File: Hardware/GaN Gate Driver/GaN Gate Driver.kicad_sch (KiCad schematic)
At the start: 12 parts, among them J1 3296W-1-102LF, U1 LT1804

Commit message: Updating Schematic
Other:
- company: (none) -> OpenEPR
- title: (none) -> GaN Gate Driver
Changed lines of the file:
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@@
 	(generator_version "8.0")
 	(paper "A4")
+	(title_block
+		(title "GaN Gate Driver")
+		(date "2024-06-16")
+		(rev "v1.0")
+		(company "OpenEPR")
+		(comment 1 "Timothy Keller")
+	)
 	(junction
 		(at 50.8 60.96)

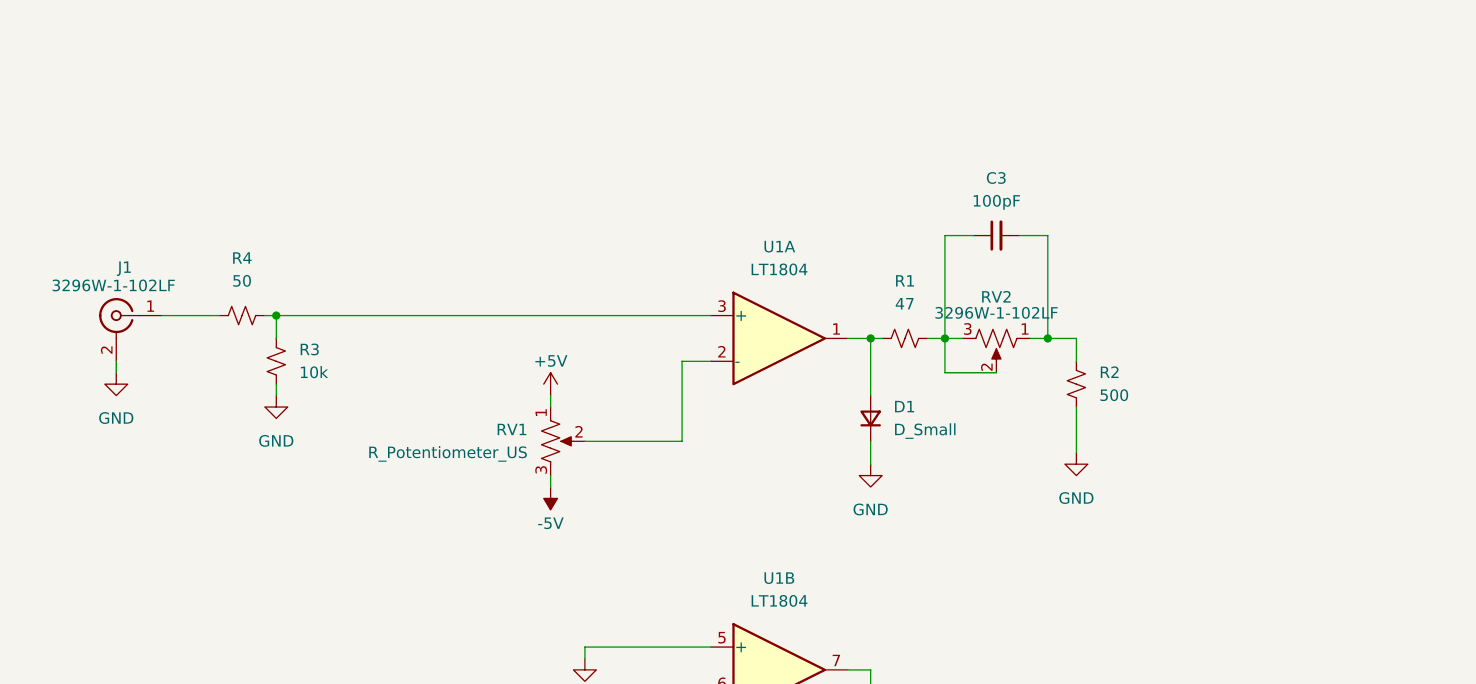
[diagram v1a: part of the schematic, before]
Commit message: Updates to gate driver
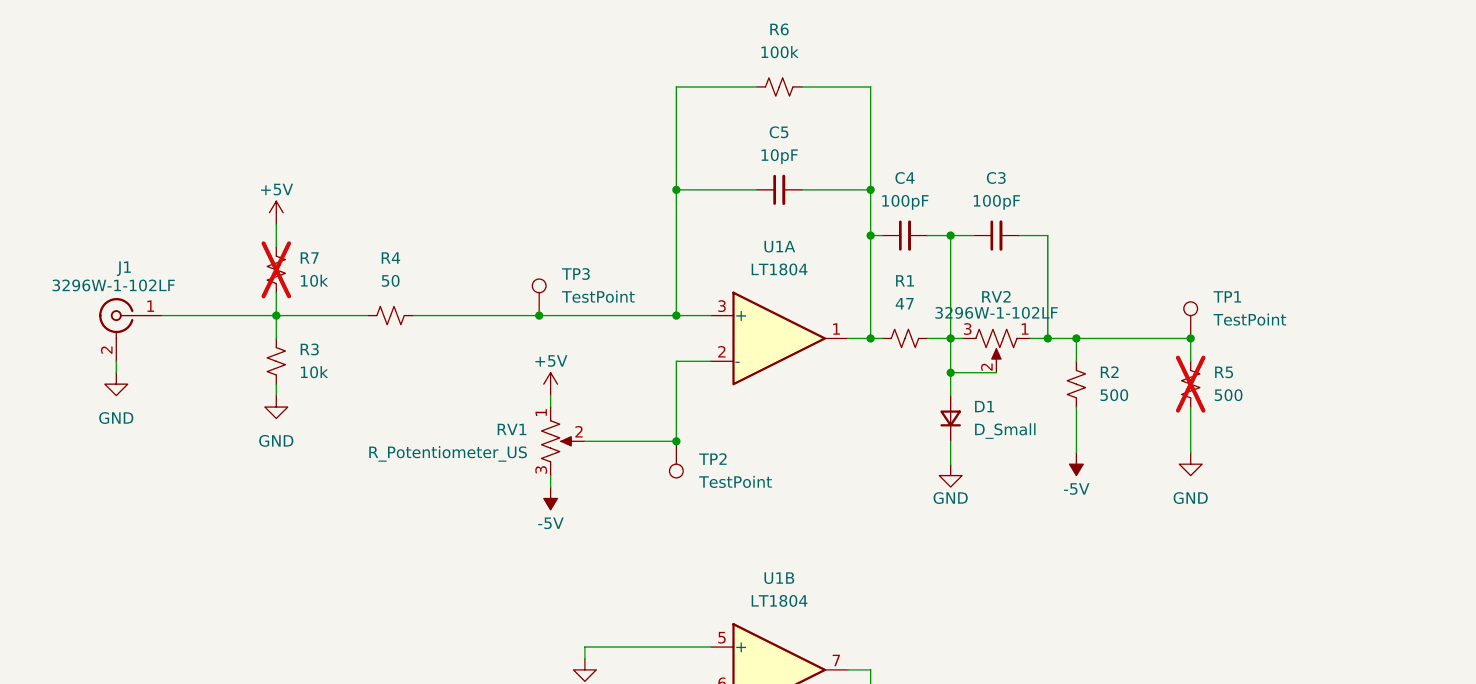
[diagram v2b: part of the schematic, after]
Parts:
- added C4: 100pF, Capacitor_SMD:C_0805_2012Metric, symbol Device:C_Small
- added C5: 10pF, Capacitor_SMD:C_0805_2012Metric, symbol Device:C_Small
- added R5: 500, Resistor_SMD:R_0805_2012Metric, symbol Device:R_Small_US
- added R6: 100k, Resistor_SMD:R_0805_2012Metric, symbol Device:R_Small_US
- added R7: 10k, Resistor_SMD:R_0805_2012Metric, symbol Device:R_Small_US
- added TP1, TP2, TP3: TestPoint, symbol Connector:TestPoint
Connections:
- net +5V: now also R7.2
- net -5V: now also R2.1
- net GND: now also R5.1; no longer R2.1
- net at R1.1, U1.1: now also C4.1, C5.2, R6.2; no longer D1.2 (A)
- net at C3.2, R2.2, RV2.1: now also R5.2, TP1.1
- net at C3.1, R1.2, RV2.2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: now also D1.2 (A), C4.2
- net at J1.1 (In), R4.1: now also R3.2, R7.1
- net at R4.2, U1.3 (+): now also C5.1, R6.1, TP3.1; no longer R3.2
- net at RV1.2, U1.2 (-): now also TP2.1
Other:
- moved on the sheet: D1, R4

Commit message: Updates to gate driver
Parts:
- added H1, H2, H3, H4: 4-40, _tim-Mounting-Holes:4-40_Hole_Pad, symbol Mechanical:MountingHole_Pad
- added J2: Conn_01x03_Socket, symbol Connector:Conn_01x03_Socket
- TP1, TP2, TP3: footprint (none) -> TestPoint:TestPoint_Pad_D1.0mm
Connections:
- net +5V: now also J2.1 (Pin_1)
- net -5V: now also J2.3 (Pin_3)
- net GND: now also H1.1, H2.1, H3.1, H4.1, J2.2 (Pin_2)

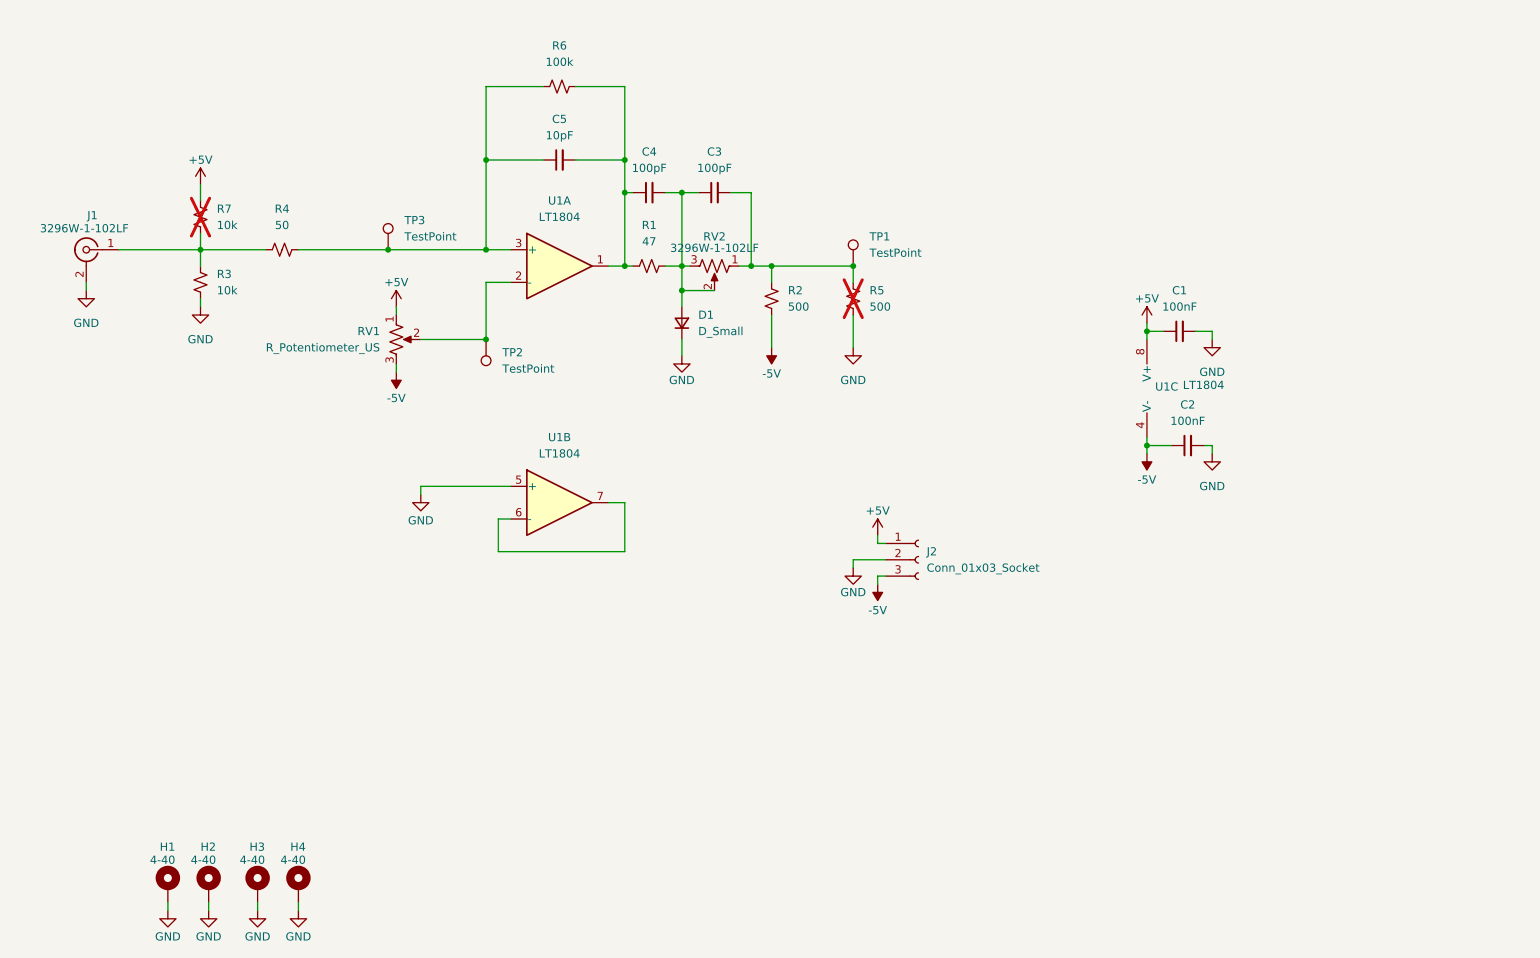
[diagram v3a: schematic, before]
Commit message: Updating gate driver board
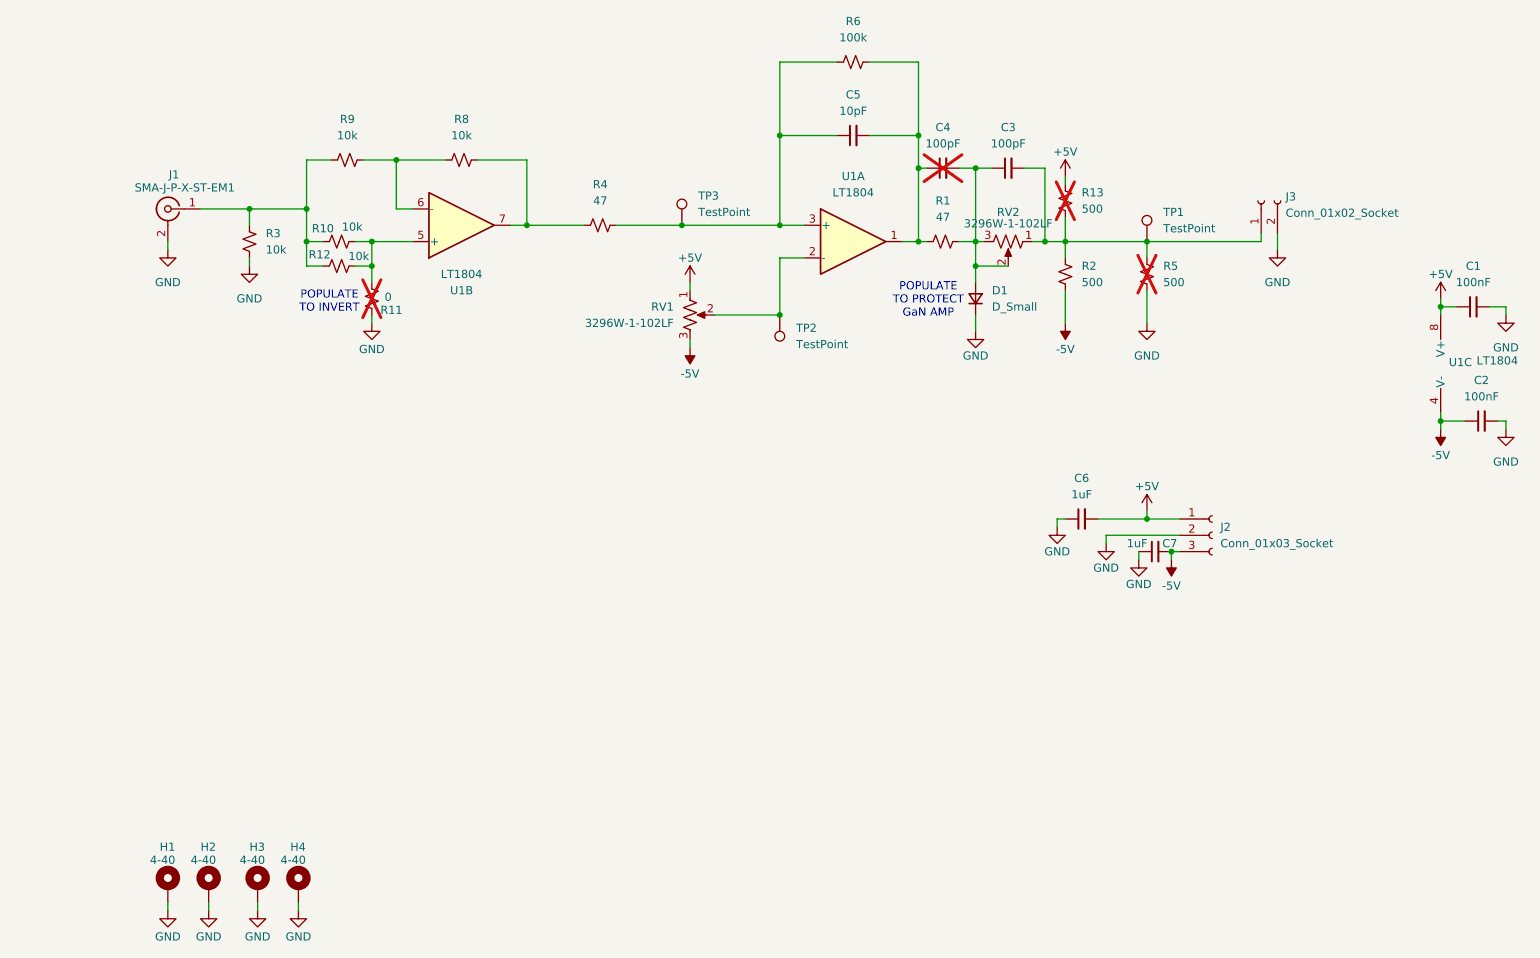
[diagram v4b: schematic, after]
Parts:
- removed R7: 10k, Resistor_SMD:R_0805_2012Metric, symbol Device:R_Small_US
- added C6, C7: 1uF, Capacitor_SMD:C_0805_2012Metric, symbol Device:C_Small
- added J3: Conn_01x02_Socket, Connector_PinSocket_2.54mm:PinSocket_1x02_P2.54mm_Vertical, symbol Connector:Conn_01x02_Socket
- added R10, R12, R8, R9: 10k, Resistor_SMD:R_0805_2012Metric, symbol Device:R_Small_US
- added R11: 0, Resistor_SMD:R_0805_2012Metric, symbol Device:R_Small_US
- added R13: 500, Resistor_SMD:R_0805_2012Metric, symbol Device:R_Small_US
- C4: now not fitted
- J1: value 3296W-1-102LF -> SMA-J-P-X-ST-EM1
- J2: footprint (none) -> Connector_PinSocket_2.54mm:PinSocket_1x03_P2.54mm_Vertical
- R4: value 50 -> 47
- RV1: value R_Potentiometer_US -> 3296W-1-102LF
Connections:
- net +5V: now also C6.2, R13.2
- net -5V: now also C7.2
- net GND: now also C6.1, C7.1, J3.2 (Pin_2), R11.1; no longer U1.5 (+)
- net at J1.1 (In), R3.2: now also R10.1, R12.1, R9.1; no longer R4.1
- net at C3.2, R2.2, R5.2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: now also J3.1 (Pin_1), R13.1
- net at U1.6 (-): now also R8.1, R9.2; no longer U1.7
- new net: R4.1, R8.2, U1.7
- new net: R10.2, R11.2, R12.2, U1.5 (+)
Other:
- note added: "POPULATE TO INVERT"
- note added: "POPULATE TO PROTECT GaN AMP"
- moved on the sheet: C1, C2, C3, C5, D1, J1, J2, R1, R2, R3, R5, R6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

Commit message: Updating board layout
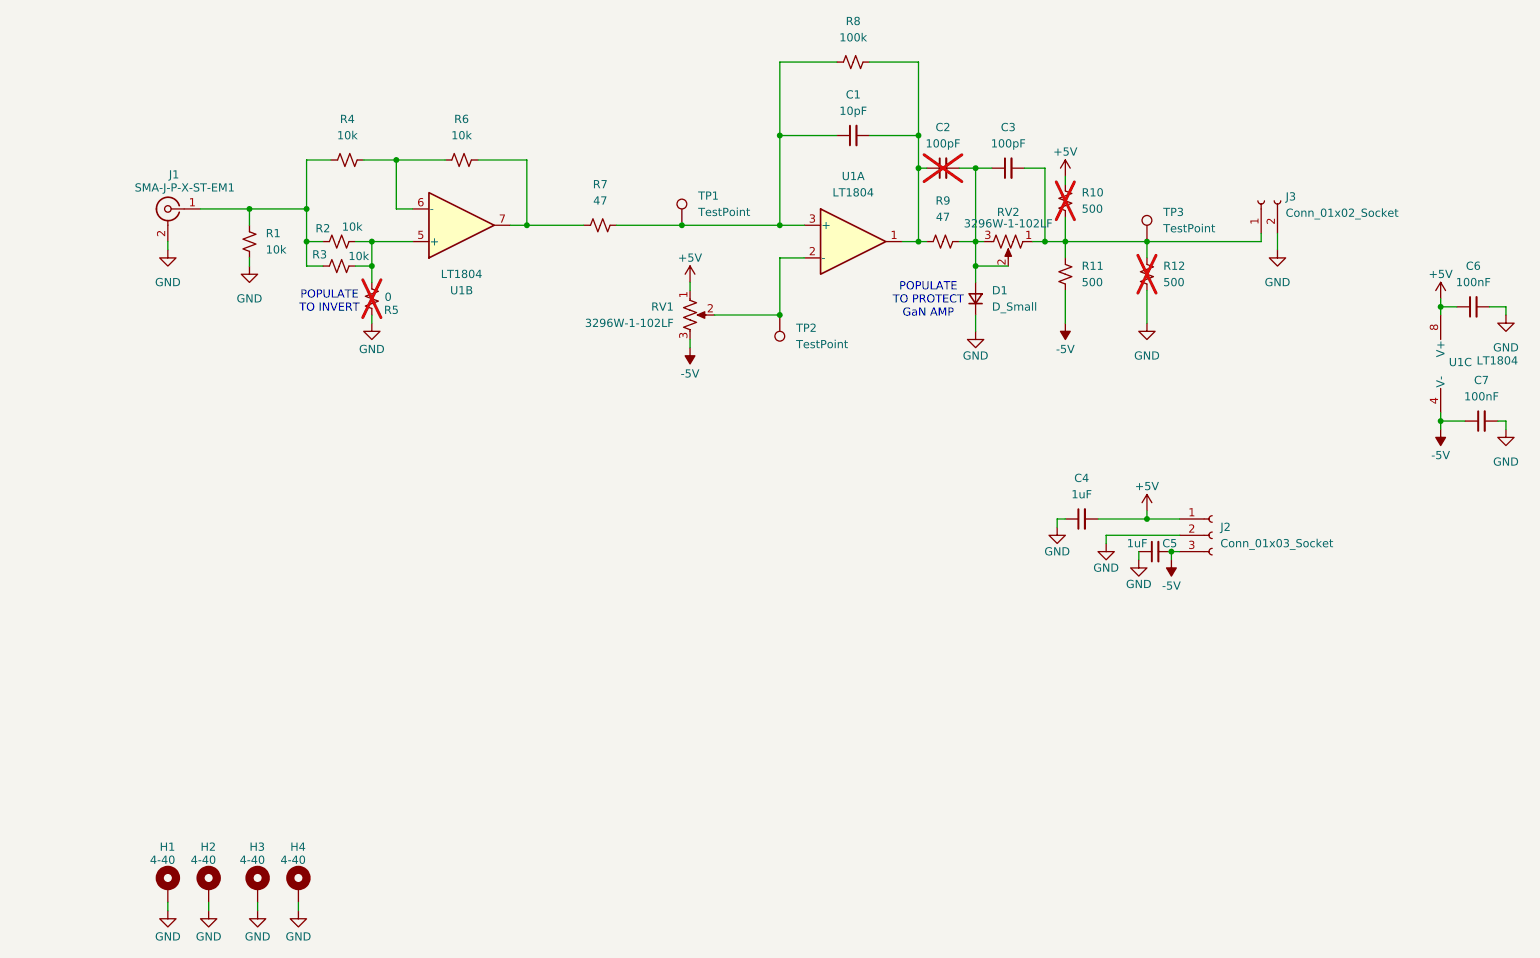
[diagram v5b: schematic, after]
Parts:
- renumbered C5 to C1, C4 to C2, C6 to C4, C7 to C5, C1 to C6, C2 to C7, R3 to R1, R13 to R10, R2 to R11, R5 to R12, R10 to R2, R12 to R3, R9 to R4, R11 to R5, R8 to R6, R4 to R7, R6 to R8, R1 to R9, TP3 to TP1, TP1 to TP3

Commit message: Adding gerbers
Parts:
- D1: value D_Small -> 1N5819HW-7-F; Digikey (none) -> 1N5819HW-FDICT-ND
- RV1, RV2: Digikey (none) -> 3296W-102LF-ND
- U1: Digikey (none) -> LT1804CS8#PBF-ND
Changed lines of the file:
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@@
 		(on_board yes)
 		(dnp no)
-		(fields_autoplaced yes)
 		(property "Reference" "D1"
 			(at 173.99 67.3099 90)
@@
 			)
 		)
-		(property "Value" "D_Small"
-			(at 173.99 69.8499 90)
+		(property "Value" "1N5819HW-7-F"
+			(at 167.386 71.882 90)
 			(effects
 				(font
@@
 		(property "Sim.Pins" "1=K 2=A"
 			(at 171.45 68.58 0)
+			(effects
+				(font
+					(size 1.27 1.27)
+				)
+				(hide yes)
+			)
+		)
+		(property "Digikey" "1N5819HW-FDICT-ND"
+			(at 171.45 68.58 90)
 			(effects
 				(font
@@
 			)
 		)
+		(property "Digikey" "3296W-102LF-ND"
+			(at 176.53 59.69 0)
+			(effects
+				(font
+					(size 1.27 1.27)
+				)
+				(hide yes)
+			)
+		)
 		(pin "1"
 		)
@@
 			)
 		)
+		(property "Digikey" "LT1804CS8#PBF-ND"
+			(at 246.38 78.74 0)
+			(effects
+				(font
+					(size 1.27 1.27)
+				)
+				(hide yes)
+			)
+		)
 		(pin "4"
 		)
@@
 			)
 		)
+		(property "Digikey" "3296W-102LF-ND"
+			(at 127 71.12 0)
+			(effects
+				(font
+					(size 1.27 1.27)
+				)
+				(hide yes)
+			)
+		)
 		(pin "1"
 		)
@@
 		)
 		(property "Description" "Single/Dual/Quad 100V/µs, 85MHz, Rail-to-Rail Input and Output Op Amps "
+			(at 152.4 59.69 0)
+			(effects
+				(font
+					(size 1.27 1.27)
+				)
+				(hide yes)
+			)
+		)
+		(property "Digikey" "LT1804CS8#PBF-ND"
 			(at 152.4 59.69 0)
 			(effects
@@
 			(at 91.44 57.15 0)
 			(effects
+				(font
+					(size 1.27 1.27)
+				)
+				(hide yes)
+			)
+		)
+		(property "Digikey" "LT1804CS8#PBF-ND"
+			(at 91.44 57.15 0)
+			(effects
